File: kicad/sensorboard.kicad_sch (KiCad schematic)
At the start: 2 parts, among them U3 TMP117MAIDRVT, U4 HDC2010YPAR

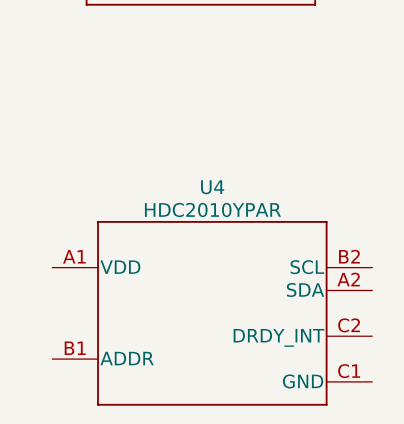
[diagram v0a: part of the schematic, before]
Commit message: Kosteussensori ja regulaattori footprintit
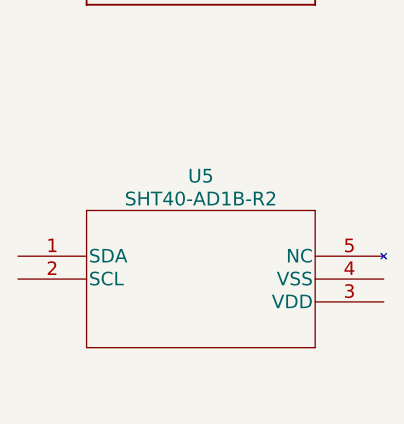
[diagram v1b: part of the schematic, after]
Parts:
- removed U4: HDC2010YPAR, YPA0006ABAB, symbol HDC2010YPAR:HDC2010YPAR
- added U5: SHT40-AD1B-R2, SHT4x_SEN, symbol SHT40-AD1B-R2:SHT40-AD1B-R2
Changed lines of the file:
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@@
 (kicad_sch (version 20230121) (generator eeschema)
   (paper "A4")
+  (symbol (lib_id "SHT40-AD1B-R2:SHT40-AD1B-R2") (at 120.65 101.6 0) (unit 1)
+    (in_bom yes) (on_board yes) (dnp no) (fields_autoplaced)
+    (property "Reference" "U5" (at 140.97 92.71 0)
+      (effects (font (size 1.524 1.524)))
+    )
+    (property "Value" "SHT40-AD1B-R2" (at 140.97 95.25 0)
+      (effects (font (size 1.524 1.524)))
+    )
+    (property "Footprint" "SHT4x_SEN" (at 140.97 95.504 0)
+      (effects (font (size 1.524 1.524)) hide)
+    )
+    (property "Datasheet" "" (at 120.65 101.6 0)
+      (effects (font (size 1.524 1.524)))
+    )
+    (pin "1")
+    (pin "2")
+    (pin "3")
+    (pin "4")
+    (pin "5")
+    (instances
+      (project "IoT_sulari"
+        (path "/184b47ed-2c2b-4c02-be35-d18f4f4e5685/ce4dfdb9-1dc9-45f7-82b8-487b1ef6453b"
+          (reference "U5") (unit 1)
+        )
+      )
+    )
+  )
   (symbol (lib_id "TMP117MAIDRVT:TMP117MAIDRVT") (at 140.97 60.96 0) (unit 1)
     (in_bom yes) (on_board yes) (dnp no) (fields_autoplaced)
@@
         )
       )
-    )
-  )
-  (symbol (lib_id "HDC2010YPAR:HDC2010YPAR") (at 142.24 107.95 0) (unit 1)
-    (in_bom yes) (on_board yes) (dnp no) (fields_autoplaced)
-    (property "Reference" "U4" (at 142.24 93.98 0)
-      (effects (font (size 1.524 1.524)))
-    )
-    (property "Value" "HDC2010YPAR" (at 142.24 96.52 0)
-      (effects (font (size 1.524 1.524)))
-    )
-    (property "Footprint" "YPA0006ABAB" (at 142.24 109.474 0)
-      (effects (font (size 1.524 1.524)) hide)
-    )
-    (property "Datasheet" "" (at 142.24 107.95 0)
-      (effects (font (size 1.524 1.524)))
-    )
-    (pin "A1")
-    (pin "A2")
-    (pin "B1")
-    (pin "B2")
-    (pin "C1")
-    (pin "C2")
-    (instances
-      (project "IoT_sulari"
-        (path "/184b47ed-2c2b-4c02-be35-d18f4f4e5685/ce4dfdb9-1dc9-45f7-82b8-487b1ef6453b"
-          (reference "U4") (unit 1)
-        )
-      )

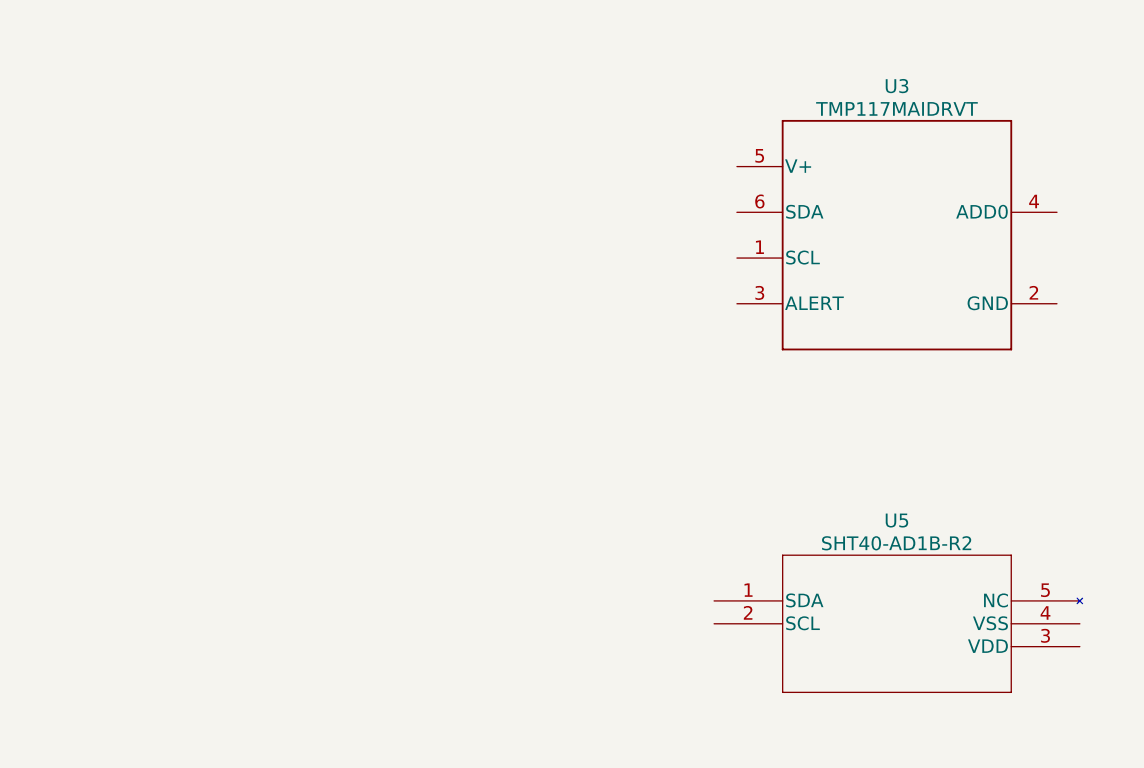
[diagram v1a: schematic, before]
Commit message: sensorboard modification, regulator modification, datasheets
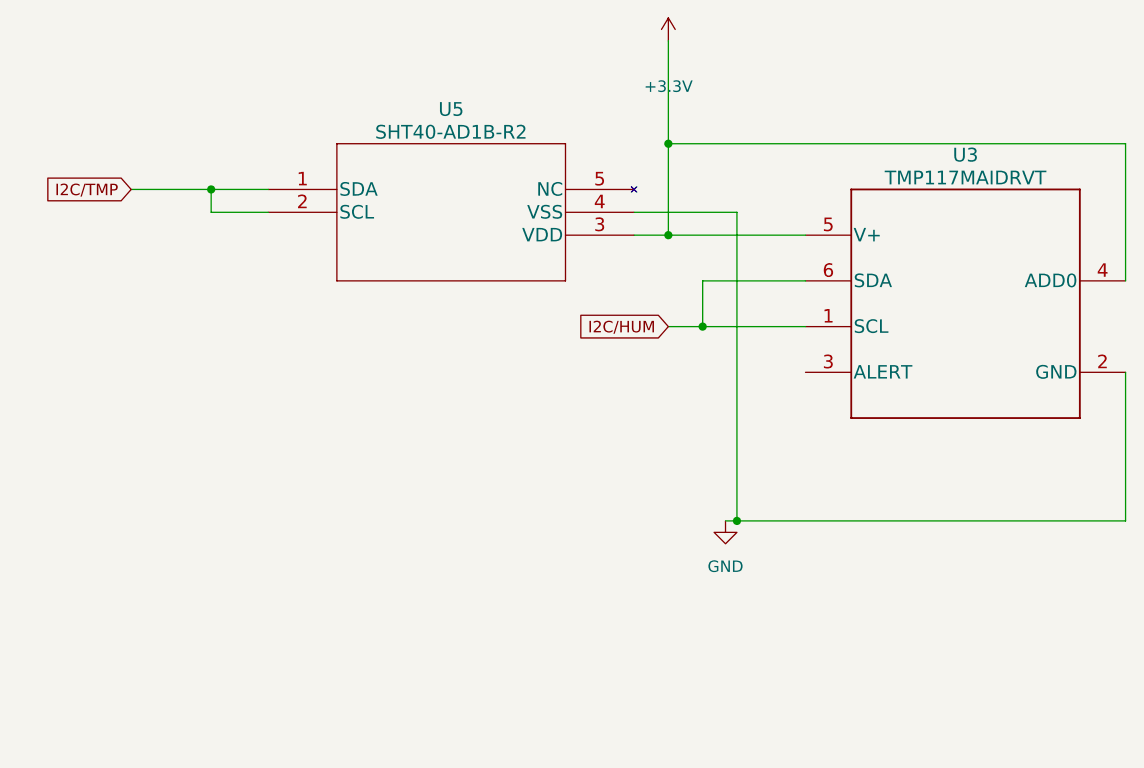
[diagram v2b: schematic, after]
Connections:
- net I2C/TMP: now reaches U5.1 (SDA)
- net I2C/TMP: now also U5.2 (SCL)
- net +3.3V: now reaches U5.3 (VDD)
- net +3.3V: now also U3.4 (ADD0), U3.5 (V+)
- net GND: now reaches U5.4 (VSS)
- net GND: now also U3.2 (GND)
- net I2C/HUM: now reaches U3.1 (SCL)
- net I2C/HUM: now also U3.6 (SDA)
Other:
- moved on the sheet: U3, U5
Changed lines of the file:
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@@
 (kicad_sch (version 20230121) (generator eeschema)
   (paper "A4")
-  (symbol (lib_id "SHT40-AD1B-R2:SHT40-AD1B-R2") (at 120.65 101.6 0) (unit 1)
+  (junction (at 119.38 71.12) (diameter 0) (color 0 0 0 0)
+  )
+  (junction (at 64.77 55.88) (diameter 0) (color 0 0 0 0)
+  )
+  (junction (at 115.57 50.8) (diameter 0) (color 0 0 0 0)
+  )
+  (junction (at 123.19 92.71) (diameter 0) (color 0 0 0 0)
+  )
+  (junction (at 115.57 60.96) (diameter 0) (color 0 0 0 0)
+  )
+  (wire (pts (xy 64.77 55.88) (xy 71.12 55.88))
+    (stroke (width 0) (type default))
+  )
+  (wire (pts (xy 123.19 58.42) (xy 123.19 92.71))
+    (stroke (width 0) (type default))
+  )
+  (wire (pts (xy 123.19 92.71) (xy 121.92 92.71))
+    (stroke (width 0) (type default))
+  )
+  (wire (pts (xy 115.57 39.37) (xy 115.57 50.8))
+    (stroke (width 0) (type default))
+  )
+  (wire (pts (xy 71.12 58.42) (xy 64.77 58.42))
+    (stroke (width 0) (type default))
+  )
+  (wire (pts (xy 166.37 92.71) (xy 123.19 92.71))
+    (stroke (width 0) (type default))
+  )
+  (wire (pts (xy 166.37 66.04) (xy 166.37 50.8))
+    (stroke (width 0) (type default))
+  )
+  (wire (pts (xy 111.76 58.42) (xy 123.19 58.42))
+    (stroke (width 0) (type default))
+  )
+  (wire (pts (xy 119.38 71.12) (xy 130.81 71.12))
+    (stroke (width 0) (type default))
+  )
+  (wire (pts (xy 115.57 50.8) (xy 115.57 60.96))
+    (stroke (width 0) (type default))
+  )
+  (wire (pts (xy 115.57 71.12) (xy 119.38 71.12))
+    (stroke (width 0) (type default))
+  )
+  (wire (pts (xy 130.81 66.04) (xy 119.38 66.04))
+    (stroke (width 0) (type default))
+  )
+  (wire (pts (xy 64.77 58.42) (xy 64.77 55.88))
+    (stroke (width 0) (type default))
+  )
+  (wire (pts (xy 55.88 55.88) (xy 64.77 55.88))
+    (stroke (width 0) (type default))
+  )
+  (wire (pts (xy 119.38 66.04) (xy 119.38 71.12))
+    (stroke (width 0) (type default))
+  )
+  (wire (pts (xy 111.76 60.96) (xy 115.57 60.96))
+    (stroke (width 0) (type default))
+  )
+  (wire (pts (xy 166.37 50.8) (xy 115.57 50.8))
+    (stroke (width 0) (type default))
+  )
+  (wire (pts (xy 115.57 60.96) (xy 130.81 60.96))
+    (stroke (width 0) (type default))
+  )
+  (wire (pts (xy 166.37 76.2) (xy 166.37 92.71))
+    (stroke (width 0) (type default))
+  )
+  (global_label "I2C{slash}TMP" (shape input) (at 55.88 55.88 180) (fields_autoplaced)
+    (effects (font (size 1.27 1.27)) (justify right))
+    (property "Intersheetrefs" "${INTERSHEET_REFS}" (at 44.8704 55.88 0)
+      (effects (font (size 1.27 1.27)) (justify right) hide)
+    )
+  )
+  (global_label "I2C{slash}HUM" (shape input) (at 115.57 71.12 180) (fields_autoplaced)
+    (effects (font (size 1.27 1.27)) (justify right))
+    (property "Intersheetrefs" "${INTERSHEET_REFS}" (at 104.137 71.12 0)
+      (effects (font (size 1.27 1.27)) (justify right) hide)
+    )
+  )
+  (symbol (lib_id "SHT40-AD1B-R2:SHT40-AD1B-R2") (at 71.12 55.88 0) (unit 1)
     (in_bom yes) (on_board yes) (dnp no) (fields_autoplaced)
-    (property "Reference" "U5" (at 140.97 92.71 0)
+    (property "Reference" "U5" (at 91.44 46.99 0)
       (effects (font (size 1.524 1.524)))
     )
-    (property "Value" "SHT40-AD1B-R2" (at 140.97 95.25 0)
+    (property "Value" "SHT40-AD1B-R2" (at 91.44 49.53 0)
       (effects (font (size 1.524 1.524)))
     )
-    (property "Footprint" "SHT4x_SEN" (at 140.97 95.504 0)
+    (property "Footprint" "SHT4x_SEN" (at 91.44 49.784 0)
       (effects (font (size 1.524 1.524)) hide)
     )
-    (property "Datasheet" "" (at 120.65 101.6 0)
+    (property "Datasheet" "" (at 71.12 55.88 0)
       (effects (font (size 1.524 1.524)))
     )
@@
     )
   )
-  (symbol (lib_id "TMP117MAIDRVT:TMP117MAIDRVT") (at 140.97 60.96 0) (unit 1)
+  (symbol (lib_id "power:GND") (at 121.92 92.71 0) (unit 1)
     (in_bom yes) (on_board yes) (dnp no) (fields_autoplaced)
-    (property "Reference" "U3" (at 140.97 44.45 0)
+    (property "Reference" "#PWR02" (at 121.92 99.06 0)
+      (effects (font (size 1.27 1.27)) hide)
+    )
+    (property "Value" "GND" (at 121.92 97.79 0)
+      (effects (font (size 1.27 1.27)))
+    )
+    (property "Footprint" "" (at 121.92 92.71 0)
+      (effects (font (size 1.27 1.27)) hide)
+    )
+    (property "Datasheet" "" (at 121.92 92.71 0)
+      (effects (font (size 1.27 1.27)) hide)
+    )
+    (pin "1")
+    (instances
+      (project "IoT_sulari"
+        (path "/184b47ed-2c2b-4c02-be35-d18f4f4e5685/900a775e-83e7-4530-ab2f-7e5f26c05ece"
+          (reference "#PWR02") (unit 1)
+        )
+        (path "/184b47ed-2c2b-4c02-be35-d18f4f4e5685/ce4dfdb9-1dc9-45f7-82b8-487b1ef6453b"
+          (reference "#PWR019") (unit 1)
+        )
+      )
+    )
+  )
+  (symbol (lib_id "TMP117MAIDRVT:TMP117MAIDRVT") (at 148.59 68.58 0) (unit 1)
+    (in_bom yes) (on_board yes) (dnp no) (fields_autoplaced)
+    (property "Reference" "U3" (at 148.59 52.07 0)
       (effects (font (size 1.524 1.524)))
     )
-    (property "Value" "TMP117MAIDRVT" (at 140.97 46.99 0)
+    (property "Value" "TMP117MAIDRVT" (at 148.59 54.61 0)
       (effects (font (size 1.524 1.524)))
     )
-    (property "Footprint" "DRV0006B" (at 140.97 62.484 0)
+    (property "Footprint" "DRV0006B" (at 148.59 70.104 0)
       (effects (font (size 1.524 1.524)) hide)
     )
-    (property "Datasheet" "" (at 140.97 60.96 0)
+    (property "Datasheet" "" (at 148.59 68.58 0)
       (effects (font (size 1.524 1.524)))
     )
@@
         )
       )
+    )
+  )
+  (symbol (lib_id "power:+3.3V") (at 115.57 39.37 0) (unit 1)
+    (in_bom yes) (on_board yes) (dnp no)
+    (property "Reference" "#PWR011" (at 115.57 43.18 0)
+      (effects (font (size 1.27 1.27)) hide)
+    )
+    (property "Value" "+3.3V" (at 115.57 44.45 0)
+      (effects (font (size 1.27 1.27)))
+    )
+    (property "Footprint" "" (at 115.57 39.37 0)
+      (effects (font (size 1.27 1.27)) hide)
+    )
+    (property "Datasheet" "" (at 115.57 39.37 0)
+      (effects (font (size 1.27 1.27)) hide)
+    )
+    (pin "1")
+    (instances
+      (project "IoT_sulari"
+        (path "/184b47ed-2c2b-4c02-be35-d18f4f4e5685"
+          (reference "#PWR011") (unit 1)
+        )
+        (path "/184b47ed-2c2b-4c02-be35-d18f4f4e5685/ce4dfdb9-1dc9-45f7-82b8-487b1ef6453b"
+          (reference "#PWR018") (unit 1)
+        )
+      )
